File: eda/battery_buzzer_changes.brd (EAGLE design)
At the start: 47 x 26.7 mm, 20 parts, among them Q2 IRFML8244

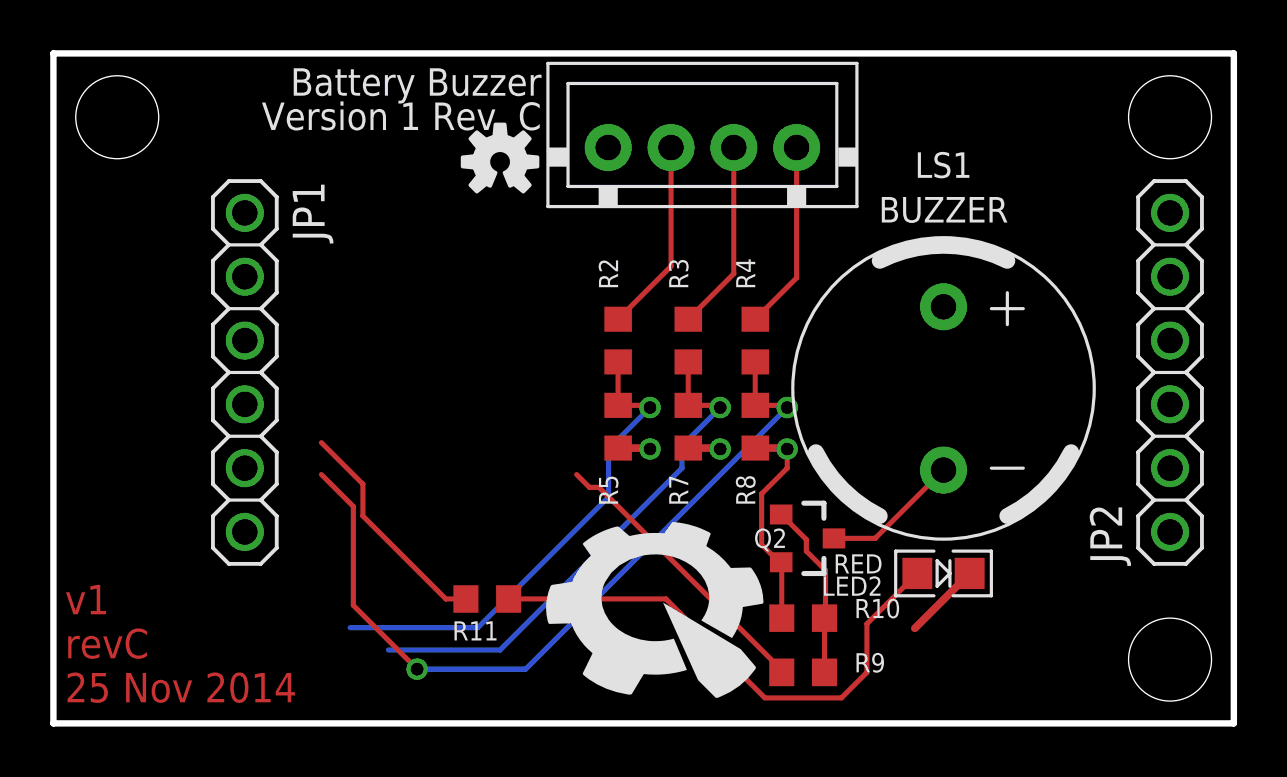
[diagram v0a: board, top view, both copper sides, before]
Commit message: Battery Buzzer Changes
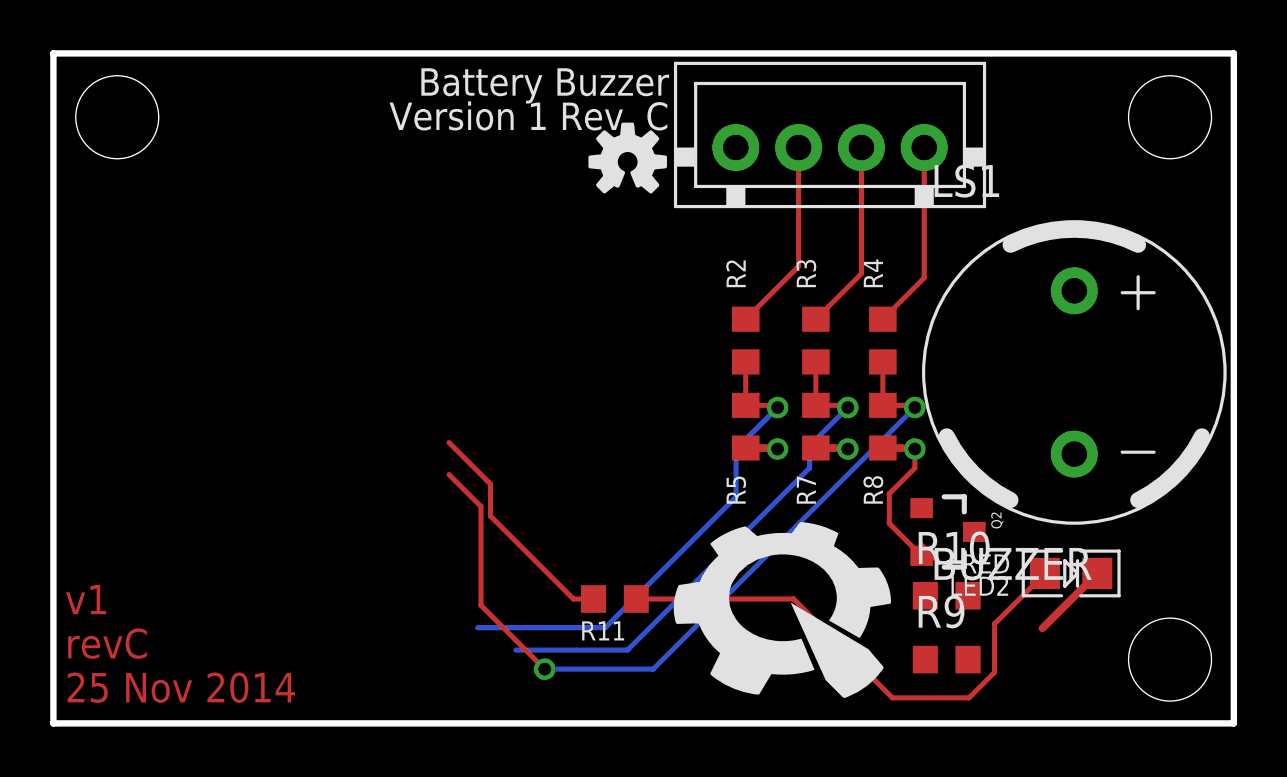
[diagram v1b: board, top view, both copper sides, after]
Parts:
- removed JP1, JP2: (no value), pie:1X06
- moved R10 5.78 mm to (35.6, 5.08)
- moved R9 5.74 mm to (35.6, 2.54)
- moved Q2 5.59 mm to (35.6, 7.62)
- moved LS1 5.25 mm to (40.6, 14.0)
- moved R11 5.08 mm to (22.4, 4.95)
- moved R2 5.08 mm to (27.6, 15.2)
- moved R3 5.08 mm to (30.4, 15.2)
- moved R4 5.08 mm to (33.0, 15.2)
- moved R5 5.08 mm to (27.6, 11.8)
- moved R7 5.08 mm to (30.4, 11.8)
- moved R8 5.08 mm to (33.0, 11.8)
- moved LED2 5.08 mm to (40.5, 5.97)
- moved U$1 5.08 mm to (29.3, 4.83)
- moved U$11 5.08 mm to (31.1, 23.1)
- moved U$7 5.08 mm to (22.9, 22.4)
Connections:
- net 5V: no longer JP2.1
- net IO0: no longer JP2.2
- net IO1: no longer JP2.3
- net IO2: no longer JP2.4
- net IO3: no longer JP2.5
- net LED_BUZZER: no longer JP1.6
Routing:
- net IO0: track 11.6 -> 0.00 mm
- net N$6: track 7.34 -> 0.00 mm
- net N$5: track 5.49 -> 0.00 mm
- net GND: track 14.7 -> 13.1 mm
